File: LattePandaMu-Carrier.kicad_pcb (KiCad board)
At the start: 4 copper layers, 165 x 100 mm, 216 parts, among them J1 Conn_01x03_Pin, J10 Conn_01x03_Pin, J11 Conn_01x03_Pin, J12 Conn_01x04_Pin, J13 Conn_01x04_Pin, J14 Conn_01x03_Pin, J15 Bus_M.2_Socket_M, J16 Bus_M.2_Socket_E, J17 Barrel_Jack_Switch, J18 USB_C_Receptacle_USB2.0_16P, J19 Conn_01x04_Pin, J20 Conn_01x04_Pin, J21 Conn_01x04_Pin, J3 HDMI_A, J4 USB3_A_Stacked, J5 USB_A_Stacked, J6 RJ45_RB1-125B8G1A, J7 Conn_01x04_Pin, J8 Conn_01x03_Pin, J9 Conn_01x04_Pin, M1 Fan_4pin, Q1 2SK3018, Q2 2SK3018, Q3 2SK3018, Q4 2SK3018, Q8 2N7002, SW1 SW_Push, SW2 SW_Push, U1 D3V3XA4B10LP, U10 ULC0524P, U11 ULC0524P, U12 ULC0524P, U14 USB PD等快充协议受电芯片-CH224K-ESSOP10, U15 LM2734X, U16 LM2734X, U17 ULC0524P, U2 D3V3XA4B10LP, U3 D3V3XA4B10LP, U4 D3V3XA4B10LP, U5 D3V3XA4B10LP, U6 RTL8111H-CG-RH, U9 ULC0524P, Y1 25MHz

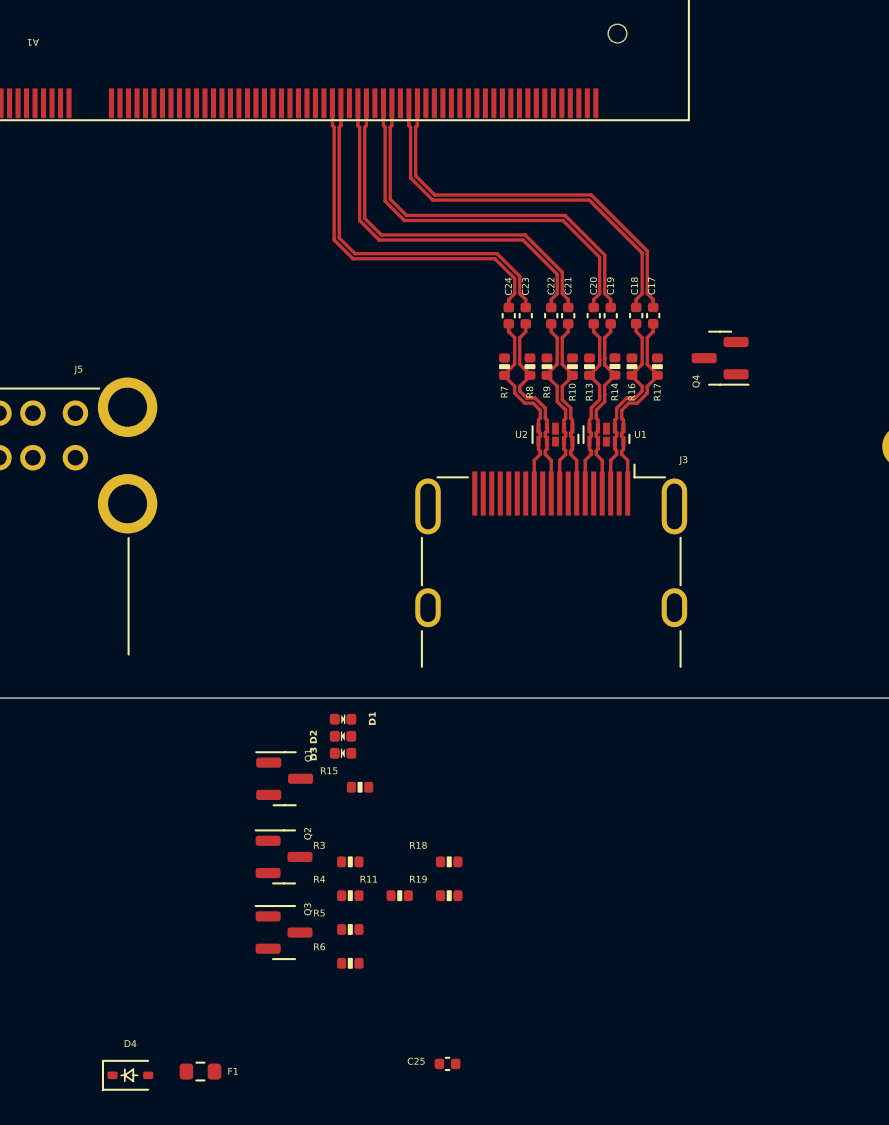
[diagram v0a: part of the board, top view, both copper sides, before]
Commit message: feat(routing): Routed hdmi signal traces and component placement.
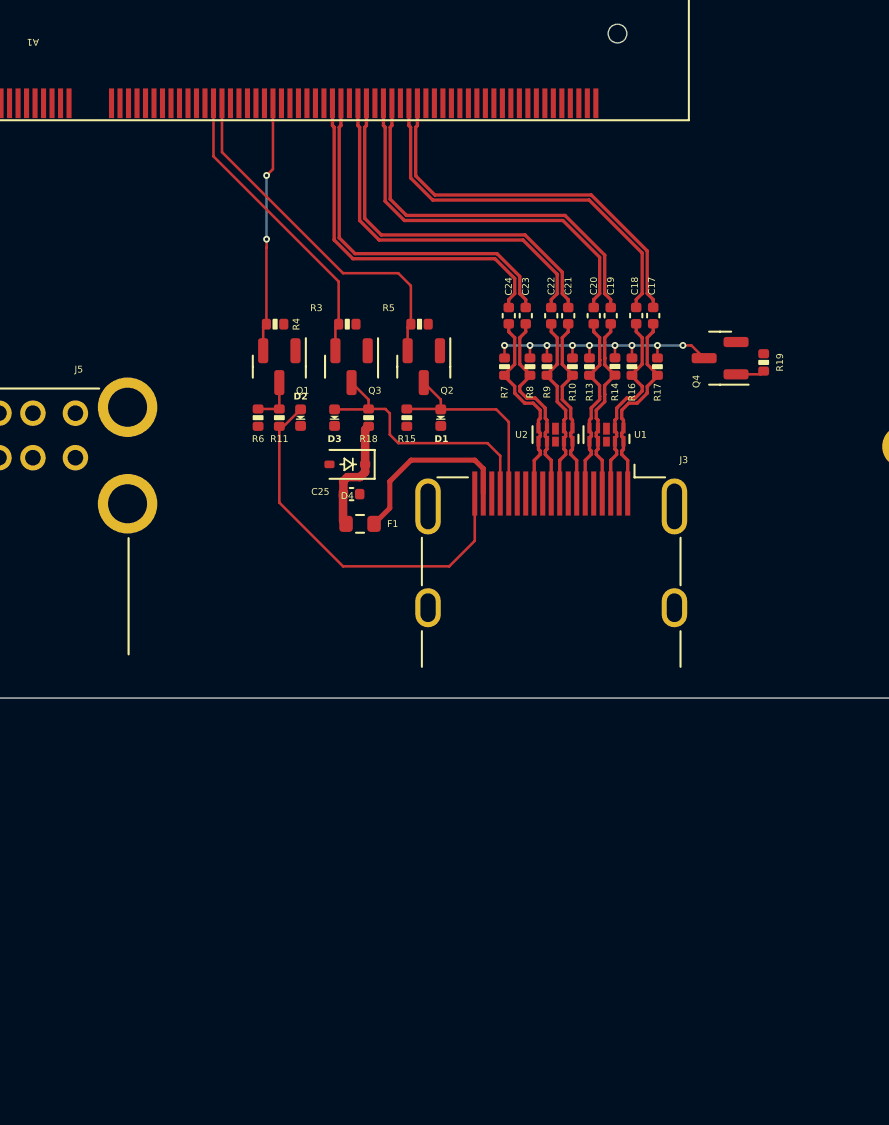
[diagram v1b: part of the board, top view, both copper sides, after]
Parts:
- moved D4 38.1 mm to (167.0, 143.8), turned to 180 degrees
- moved R19 36.4 mm to (191.5, 137.8), turned to -90 degrees
- moved R5 35.9 mm to (171.2, 135.5)
- moved C25 34.0 mm to (167.2, 145.5)
- moved R4 33.9 mm to (162.8, 135.5)
- moved F1 33.6 mm to (167.8, 147.2)
- moved Q3 33.5 mm to (167.2, 138.0), turned to -90 degrees
- moved R6 32.6 mm to (161.8, 141.0), turned to 90 degrees
- moved R3 31.6 mm to (167.0, 135.5)
- moved Q2 30.0 mm to (171.5, 138.0), turned to -90 degrees
- moved R11 29.0 mm to (163.0, 141.0), turned to 90 degrees
- moved R18 26.6 mm to (168.2, 141.0), turned to -90 degrees
- moved Q1 24.3 mm to (163.0, 138.0), turned to -90 degrees
- moved R15 21.9 mm to (170.5, 141.0), turned to -90 degrees
- moved D3 19.8 mm to (166.2, 141.0), turned to 90 degrees
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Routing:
- net /HDMI/HPD: track 0.00 -> 22.6 mm
- net /HDMI/DDI_B_DDC_SCL: track 0.00 -> 21.1 mm
- net Net-(Q4-D): track 0.00 -> 18.0 mm, vias 0 -> 9
- net /HDMI/DDI_B_DDC_SDA: track 0.00 -> 17.7 mm
- net /HDMI/DDC_SDA: track 0.00 -> 15.8 mm
- net /HDMI/DDI_B_HPD: track 0.00 -> 14.8 mm, vias 0 -> 2
- net /HDMI/DDC_SCL: track 0.00 -> 12.5 mm
- net Net-(J3-+5V): track 0.00 -> 10.2 mm
- net 5V_HDMI_VCC: track 0.00 -> 6.89 mm
- net Net-(Q1-D): track 0.00 -> 2.80 mm
- net Net-(Q4-G): track 0.00 -> 1.70 mm

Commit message: feat(routing): Routed usb 3 components.
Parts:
- moved C31 334.4 mm to (90.0, 144.8)
- moved C32 333.3 mm to (90.0, 142.8)
- moved F4 321.7 mm to (94.0, 144.8)
- moved F5 320.7 mm to (94.0, 142.8)
- moved C27 318.2 mm to (100.2, 132.0), turned to -90 degrees
- moved C26 317.7 mm to (101.2, 132.0), turned to -90 degrees
- moved C29 314.8 mm to (102.8, 132.0), turned to -90 degrees
- moved C28 314.3 mm to (103.8, 132.0), turned to -90 degrees
- moved U3 310.2 mm to (102.0, 135.2), turned to -90 degrees
- moved U5 310.1 mm to (108.0, 135.3), turned to -90 degrees
- moved D8 307.8 mm to (113.8, 152.5), turned to -90 degrees
- moved D7 307.8 mm to (113.8, 150.5), turned to 90 degrees
- moved D5 306.4 mm to (112.8, 136.0), turned to -90 degrees
- moved D6 305.6 mm to (112.8, 134.0), turned to 90 degrees
- moved C30 290.5 mm to (142.2, 160.2)
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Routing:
- net /USB 2.0 & 3.0/CON_USB3_D_P: track 0.00 -> 66.1 mm, vias 0 -> 2
- net /USB 2.0 & 3.0/CON_USB3_D_N: track 0.00 -> 66.1 mm, vias 0 -> 2
- net /USB 2.0 & 3.0/CON_USB4_D_P: track 0.00 -> 42.9 mm, vias 0 -> 1
- net /USB 2.0 & 3.0/CON_USB4_D_N: track 0.00 -> 42.5 mm, vias 0 -> 1
- net /USB 2.0 & 3.0/CON_USB3_SSRX_N: track 0.00 -> 40.8 mm, vias 0 -> 3
- net /USB 2.0 & 3.0/CON_USB3_SSRX_P: track 0.00 -> 40.3 mm, vias 0 -> 3
- net /USB 2.0 & 3.0/CON_USB4_SSRX_P: track 0.00 -> 35.4 mm, vias 0 -> 2
- net /USB 2.0 & 3.0/CON_USB4_SSRX_N: track 0.00 -> 35.3 mm, vias 0 -> 2
- net /LattePanda Module/HSIO_0_TX-: track 0.00 -> 23.8 mm
- net /LattePanda Module/HSIO_0_TX+: track 0.00 -> 23.8 mm
- net /LattePanda Module/HSIO_1_TX-: track 0.00 -> 22.8 mm
- net /LattePanda Module/HSIO_1_TX+: track 0.00 -> 22.8 mm
- net /USB 2.0 & 3.0/CON_USB3_SSTX_P: track 0.00 -> 13.0 mm, vias 0 -> 1
- net /USB 2.0 & 3.0/CON_USB3_SSTX_N: track 0.00 -> 12.8 mm, vias 0 -> 1
- net /USB 2.0 & 3.0/CON_USB4_SSTX_P: track 0.00 -> 8.06 mm
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
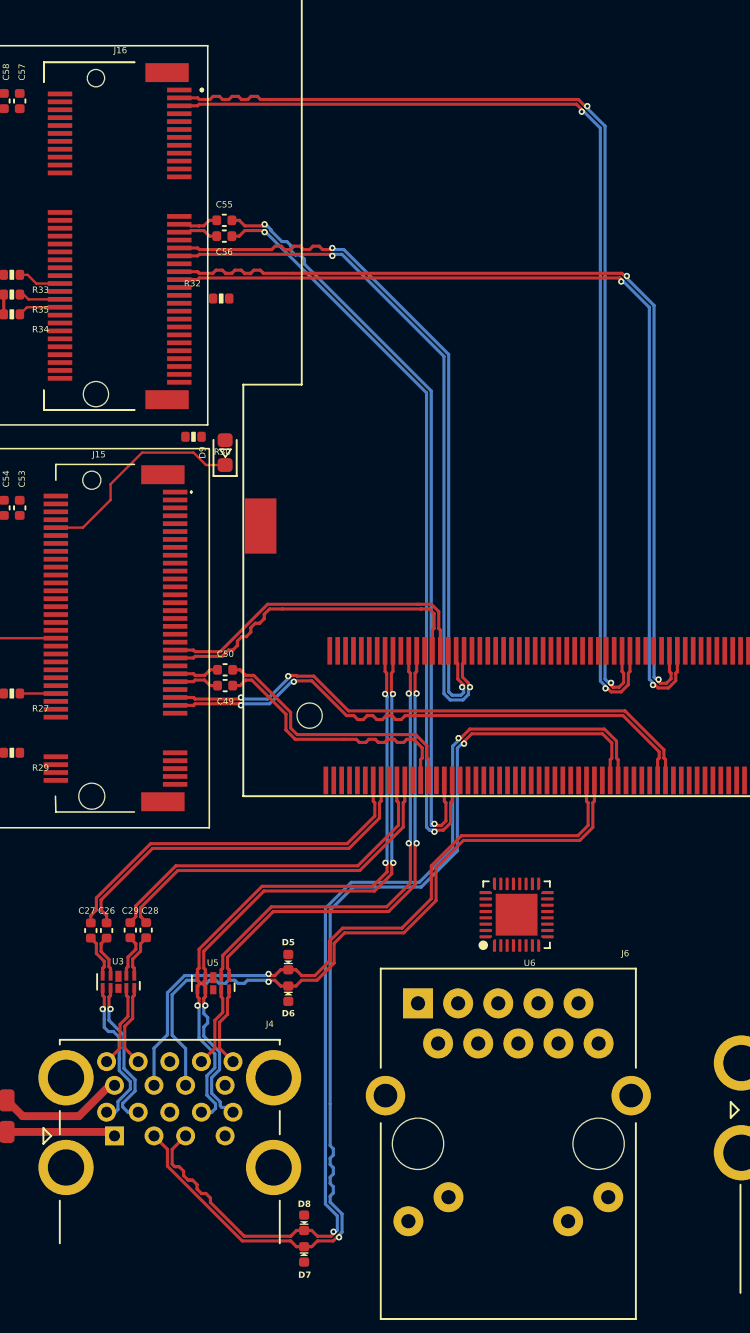
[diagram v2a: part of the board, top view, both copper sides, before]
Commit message: feat(routing): Optimized track routing.
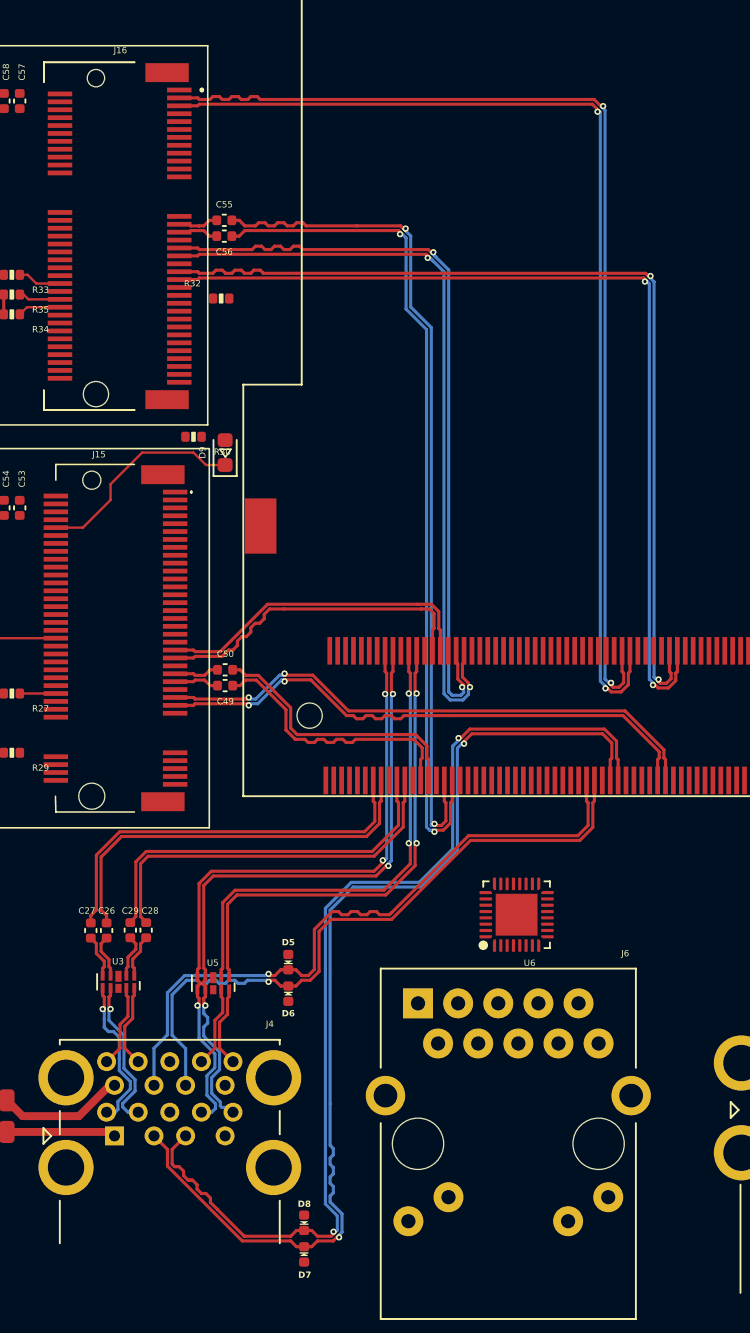
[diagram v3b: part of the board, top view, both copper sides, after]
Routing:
- net /LattePanda Module/HSIO_3_TX+: track 48.8 -> 53.9 mm
- net /LattePanda Module/HSIO_3_TX-: track 48.8 -> 53.9 mm
- net /LattePanda Module/HSIO_3_RX+: track 45.8 -> 49.2 mm
- net /LattePanda Module/HSIO_3_RX-: track 45.8 -> 49.2 mm
- net /USB 2.0 & 3.0/CON_USB3_SSRX_N: track 40.8 -> 42.7 mm
- net /USB 2.0 & 3.0/CON_USB3_SSRX_P: track 40.3 -> 42.2 mm
- net /LattePanda Module/HSIO_0_TX+: track 23.8 -> 25.6 mm
- net /LattePanda Module/HSIO_0_TX-: track 23.8 -> 25.6 mm
- net /LattePanda Module/HSIO_1_TX+: track 22.8 -> 24.5 mm
- net /LattePanda Module/HSIO_1_TX-: track 22.8 -> 24.5 mm
- net /USB 2.0 & 3.0/CON_USB4_SSRX_N: track 35.3 -> 36.5 mm
- net /USB 2.0 & 3.0/CON_USB4_SSRX_P: track 35.4 -> 36.6 mm
- net /LattePanda Module/REFCLK_3-: track 58.3 -> 59.2 mm
- net /LattePanda Module/REFCLK_3+: track 58.3 -> 59.2 mm
- net /LattePanda Module/USB_2_P7-: track 66.9 -> 67.5 mm
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
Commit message: feat(routing): Routed ethernet connections; still need to perform length tuning on differential pairs or rerouting.
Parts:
- added U7: ULC0524P, A_HDJ_Library:Diodes_UDFN-10_1.0x2.5mm_P0.5mm, F.Cu at (141.5, 133.1)
- added U8: ULC0524P, A_HDJ_Library:Diodes_UDFN-10_1.0x2.5mm_P0.5mm, F.Cu at (144.8, 133.1)
- moved C47 250.9 mm to (127.8, 140.8)
- moved C46 249.4 mm to (129.0, 135.5)
- moved Y1 248.3 mm to (127.8, 137.8)
- moved C45 245.5 mm to (129.3, 131.8)
- moved R23 245.1 mm to (126.7, 135.5)
- moved C48 244.7 mm to (133.6, 137.4), turned to 90 degrees
- moved R22 242.7 mm to (132.6, 134.4)
- moved C43 241.6 mm to (133.2, 127.8)
- moved R20 241.5 mm to (130.3, 129.8), turned to 180 degrees
- moved R21 241.5 mm to (130.3, 130.8), turned to 180 degrees
- moved C33 241.2 mm to (131.3, 132.2)
- moved C34 239.1 mm to (133.2, 132.2), turned to 180 degrees
- moved C39 238.6 mm to (133.2, 128.8)
- moved C42 237.5 mm to (137.3, 125.6), turned to -90 degrees
- moved C38 235.5 mm to (136.3, 125.6), turned to -90 degrees
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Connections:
- net Net-(U6-HSIN) renamed /Gigabit Ethernet/HSI-
- net Net-(U6-HSIP) renamed /Gigabit Ethernet/HSI+
- net Net-(U6-HSON) renamed /Gigabit Ethernet/HSO-
- net Net-(U6-HSOP) renamed /Gigabit Ethernet/HSO+
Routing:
- net /Gigabit Ethernet/LED2_ACT: track 0.00 -> 35.8 mm, vias 0 -> 1
- net /Gigabit Ethernet/GbE_PCIe_RX-: track 0.00 -> 23.6 mm, vias 0 -> 2
- net /Gigabit Ethernet/LED1_1000: track 0.00 -> 22.9 mm, vias 0 -> 1
- net /Gigabit Ethernet/GbE_PCIe_CLK-: track 0.00 -> 22.4 mm, vias 0 -> 2
- net /Gigabit Ethernet/GbE_PCIe_RX+: track 0.00 -> 22.1 mm, vias 0 -> 2
- net /Gigabit Ethernet/GbE_PCIe_CLK+: track 0.00 -> 21.4 mm, vias 0 -> 2
- net Net-(U6-CKXTAL1): track 0.00 -> 21.4 mm
- net /Gigabit Ethernet/MDI3+: track 0.00 -> 18.8 mm
- net /Gigabit Ethernet/MDI3-: track 0.00 -> 17.7 mm
- net +1V0: track 0.00 -> 17.7 mm, vias 0 -> 6
- net /Gigabit Ethernet/MDI2+: track 0.00 -> 14.7 mm
- net /Gigabit Ethernet/GbE_PCIe_TX+: track 0.00 -> 14.3 mm, vias 0 -> 2
- net Net-(J6-PadL3): track 0.00 -> 13.8 mm
- net Net-(U6-CKXTAL2): track 0.00 -> 13.4 mm
- net /Gigabit Ethernet/GbE_PCIe_TX-: track 0.00 -> 13.3 mm, vias 0 -> 2
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
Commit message: feat: Moved ethernet connector and rerouted components to allow for usb 2 routing.
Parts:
- moved F3 30.9 mm to (194.0, 142.0)
- moved F2 26.6 mm to (194.0, 144.0)
- moved U4 23.7 mm to (206.2, 137.8), turned to -90 degrees
- moved C30 18.4 mm to (192.2, 145.8)
- moved R23 6.41 mm to (120.5, 137.0)
- moved Y1 6.41 mm to (121.6, 139.3)
- moved C46 6.41 mm to (122.8, 137.0)
- moved C47 6.36 mm to (121.6, 142.1)
- moved J6 6.06 mm to (130.9, 137.0)
- moved R22 6.05 mm to (126.6, 135.2)
- moved C48 5.90 mm to (127.7, 137.4)
- moved R24 5.61 mm to (147.0, 148.0)
- moved R25 5.60 mm to (147.0, 149.0)
- moved C39 4.73 mm to (128.5, 128.3)
- moved C43 4.73 mm to (128.5, 127.3)
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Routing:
- net /USB 2.0 & 3.0/CON_USB1_D_P: track 0.00 -> 93.8 mm, vias 0 -> 2
- net /USB 2.0 & 3.0/CON_USB1_D_N: track 0.00 -> 93.8 mm, vias 0 -> 2
- net /USB 2.0 & 3.0/CON_USB2_D_P: track 0.00 -> 93.7 mm, vias 0 -> 2
- net /USB 2.0 & 3.0/CON_USB2_D_N: track 0.00 -> 93.7 mm, vias 0 -> 2
- net Net-(J5-VBUS2): track 0.00 -> 12.1 mm
- net Net-(J5-VBUS1): track 0.00 -> 6.37 mm
- net /Gigabit Ethernet/GbE_PCIe_TX-: track 13.3 -> 8.38 mm
- net /Gigabit Ethernet/GbE_PCIe_TX+: track 14.3 -> 9.37 mm
- net /Gigabit Ethernet/GbE_PCIe_RX+: track 22.1 -> 26.6 mm
- net Net-(U6-CKXTAL2): track 13.4 -> 17.3 mm
- net /~{PLT_RST}: track 12.1 -> 15.9 mm
- net +5V: track 3.57 -> 7.34 mm
- net GND: track 3.41 -> 0.00 mm
- net /Gigabit Ethernet/GbE_PCIe_RX-: track 23.6 -> 26.6 mm
- net Net-(U6-CKXTAL1): track 21.4 -> 23.7 mm
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
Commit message: feat(routing): Routed remaining m.2 interfaces.
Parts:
- moved R46 152.0 mm to (185.8, 90.5), turned to 180 degrees
- moved JP1 6.13 mm to (188.8, 92.8), turned to 180 degrees
- moved R32 0.56 mm to (108.8, 91.5)
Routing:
- net /LattePanda Module/SUSCLK_WIFI: track 0.00 -> 127.8 mm, vias 0 -> 4
- net /~{PEWAKE}: track 0.00 -> 96.8 mm, vias 0 -> 4
- net /~{PLT_RST}: track 15.9 -> 110.0 mm, vias 2 -> 7
- net /M.2 M Key/~{CLKREQE}: track 0.00 -> 2.51 mm
- net Net-(J15-SUSCLK): track 0.00 -> 2.38 mm
- net Net-(D9-A): track 0.00 -> 1.58 mm

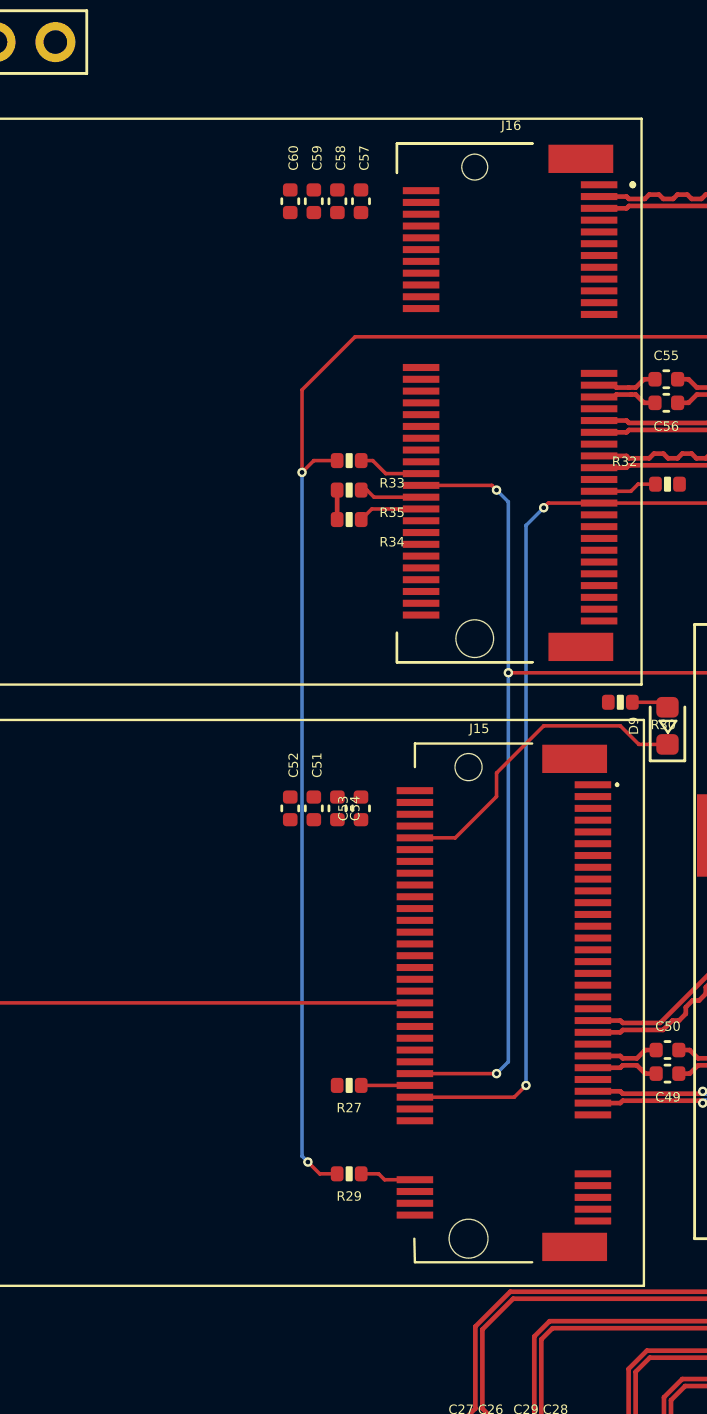
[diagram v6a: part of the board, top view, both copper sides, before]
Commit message: feat: Routed remaining m.2 passives and power.
- Fixed capacitor values.
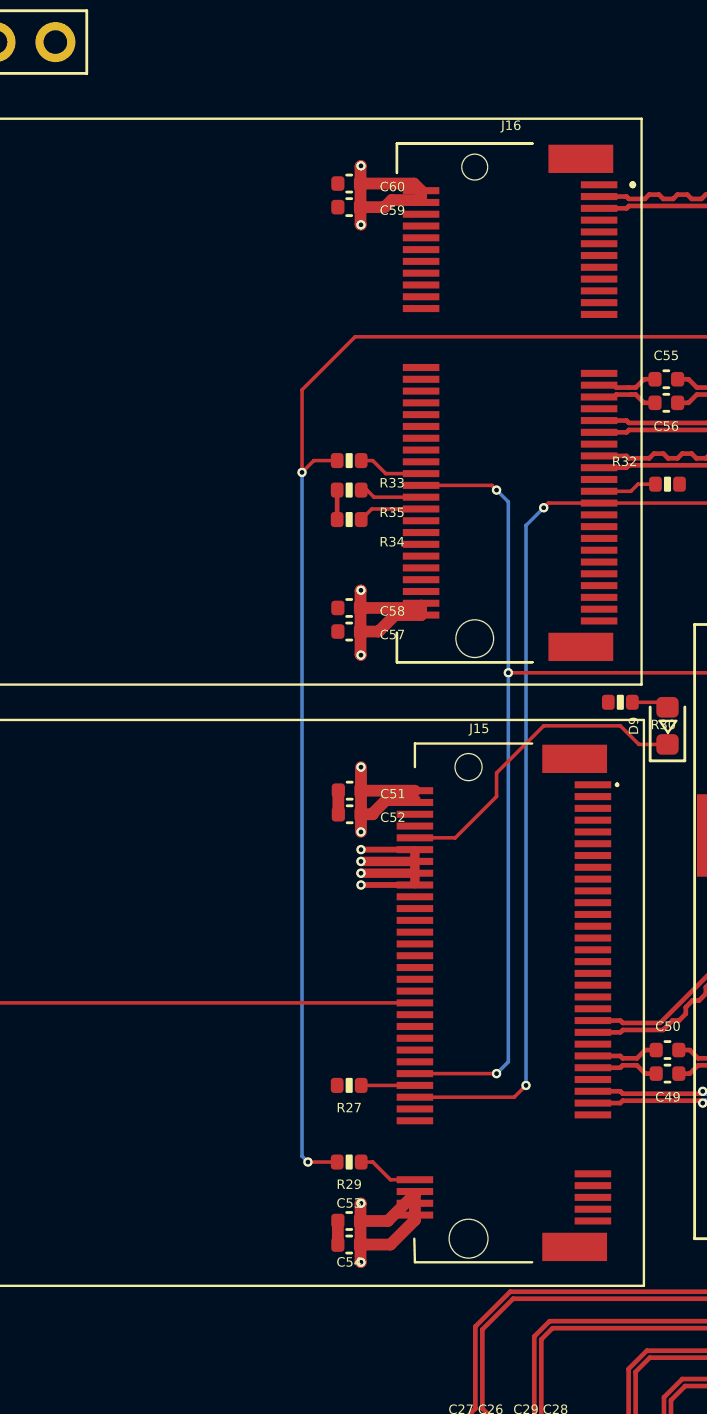
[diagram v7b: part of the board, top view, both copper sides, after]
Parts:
- C51, C53, C57, C59: value 100nF/50V -> 10uF/10V
- moved C54 18.5 mm to (95.2, 123.8), turned to 180 degrees
- moved C57 18.3 mm to (95.2, 97.8), turned to 180 degrees
- moved C53 17.5 mm to (95.2, 122.8), turned to 180 degrees
- moved C58 17.3 mm to (95.2, 96.8), turned to 180 degrees
- moved C60 2.61 mm to (95.2, 78.8), turned to 180 degrees
- moved C52 2.53 mm to (95.3, 105.5), turned to 180 degrees
- moved C51 1.69 mm to (95.3, 104.5), turned to 180 degrees
- moved C59 1.52 mm to (95.2, 79.8), turned to 180 degrees
- moved R29 0.50 mm to (95.2, 120.2)
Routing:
- net +3.3V: track 14.9 -> 105.9 mm, vias 0 -> 12
- net GND: track 0.00 -> 2.00 mm
